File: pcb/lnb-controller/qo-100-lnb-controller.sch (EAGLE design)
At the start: 170 parts, among them CON1 3P-SH-SIDE, CON2 2EDG-2P-5MM, U1 EFM32PG1B100F256GM32, U10 ADP7142AUJZ-3.3, U2 TX-8010-EAW-1070-25M0000000, U3 DSB321SDA, U4 SI5351C-B-GM, U5 LT8650S-1, U6 AD5272-100, U7 AD5272-100, U8 MIC23155, U9 LT8636

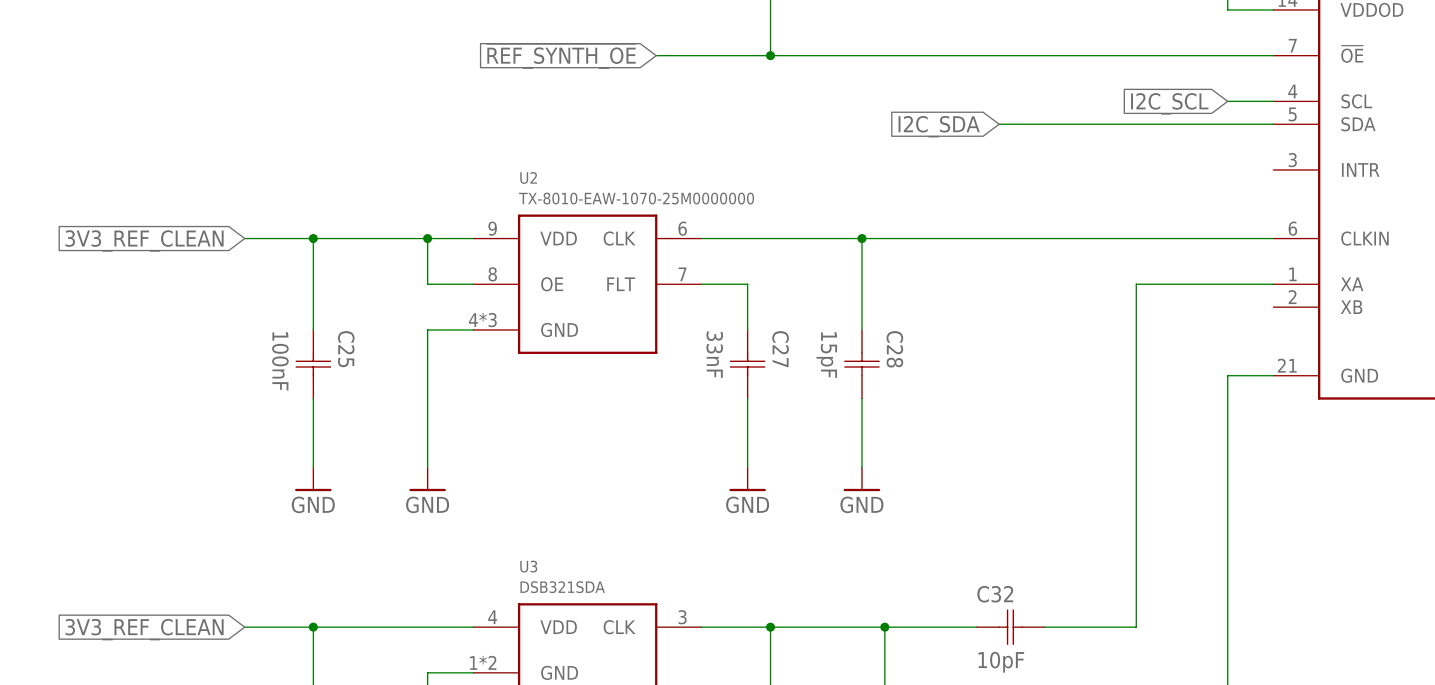
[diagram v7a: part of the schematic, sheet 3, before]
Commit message: Nothing to do on LNB Controller
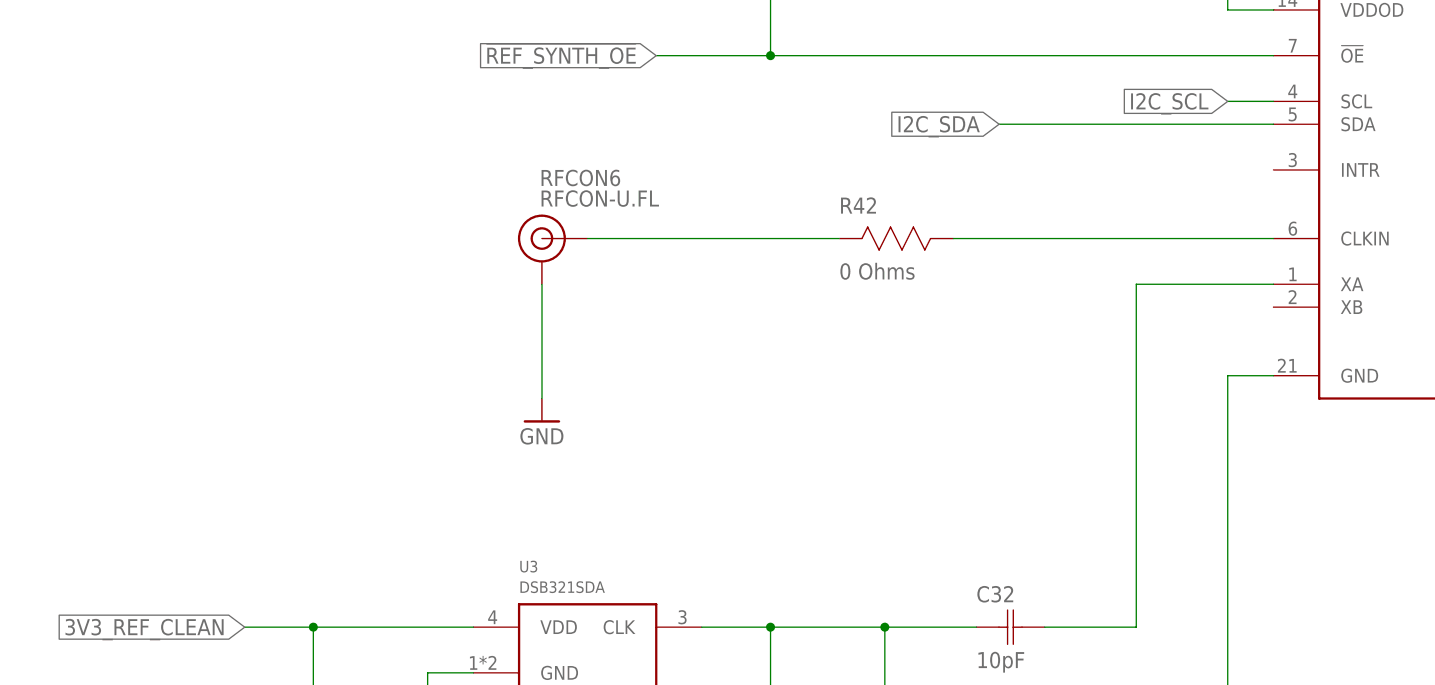
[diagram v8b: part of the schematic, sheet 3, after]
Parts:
- removed C25: 100nF, Capacitor:CAPACITOR-0603
- removed C27: 33nF, Capacitor:CAPACITOR-0603
- removed C28: 15pF, Capacitor:CAPACITOR-0603
- removed U2: TX-8010-EAW-1070-25M0000000, Microchip:TX-8010-EAW-1070-25M0000000
- added R42: 0 Ohms, Resistor:RESISTOR-0603
- added RFCON6: RFCON-U.FL, RF Connector:RFCON-U.FL
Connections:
- net N$41 renamed EXT_REF_OUT
- removed net N$21: C27.C1, U2.FLT
- new net EXT_REF_IN: R42.2, RFCON6.SIGNAL
- net 3V3: no longer C51.C1, C53.C1, C61.C1, C62.C1, U6.!RESET, U6.ADDR, U6.VDD, U7.!RESET, U7.VDD
- net 3V3_REF_CLEAN: no longer C25.C1, U2.OE, U2.VDD
- net 5V0: now also C51.C1, C53.C1, C61.C1, C62.C1, U6.!RESET, U6.ADDR, U6.VDD, U7.!RESET, U7.VDD
- net GND: now also RFCON6.GND; no longer C25.C2, C27.C2, C28.C2, U2.GND
- net N$37: now also R42.1; no longer C28.C1, U2.CLK
